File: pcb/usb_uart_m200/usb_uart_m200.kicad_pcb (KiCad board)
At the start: 2 copper layers, 25 x 25.1 mm, 17 parts, among them J1 Conn_01x02_Socket, P1 USB_C_Plug_USB2.0, U1 CY7C65213-28PVXI, U2 MIC5317-3.3xM5, U4 USBLC6-2SC6, X1 2059-301_998-403

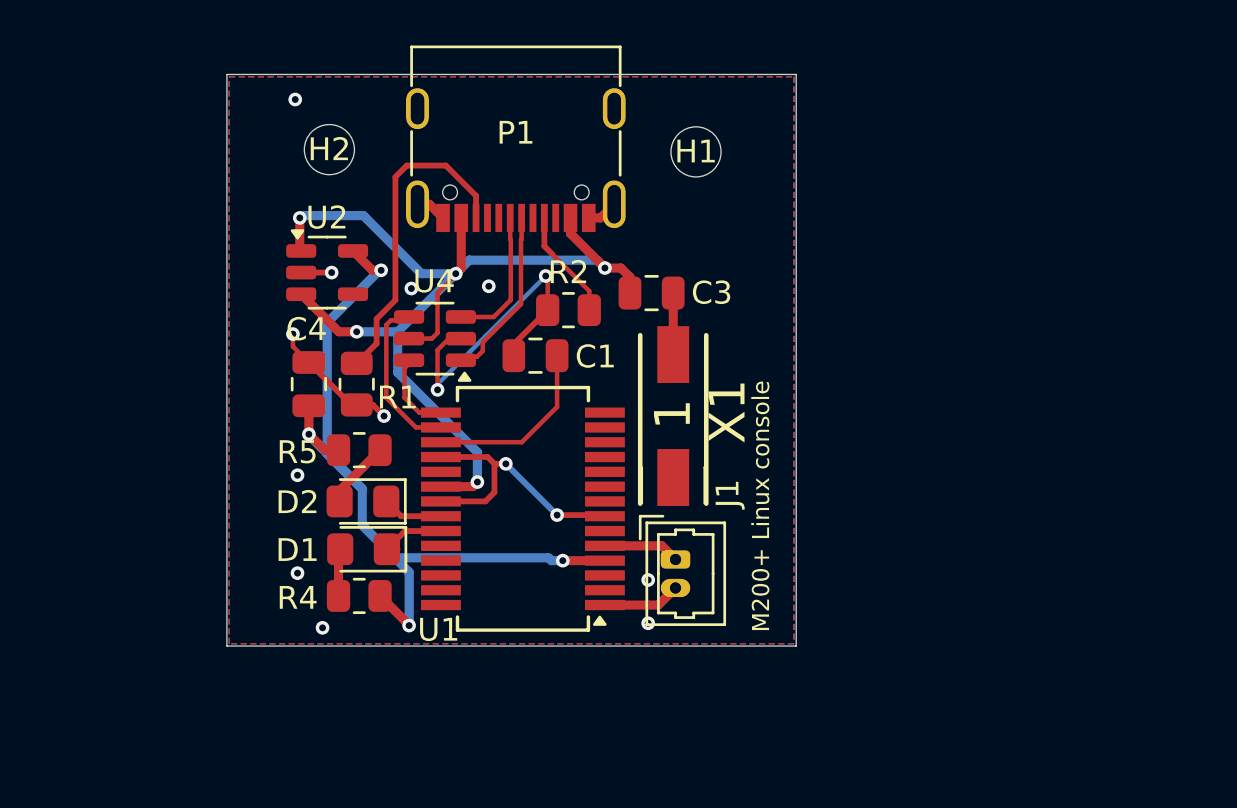
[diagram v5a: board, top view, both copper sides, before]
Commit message: Updating the uart and fel mode adapter after soldering it.
Manufacturing shiwed the pcb to be too large and the gnd wire connector
too close to the uart connector. The farnell reference resistor on the
fel mode adapter was of the wrong foorprint.
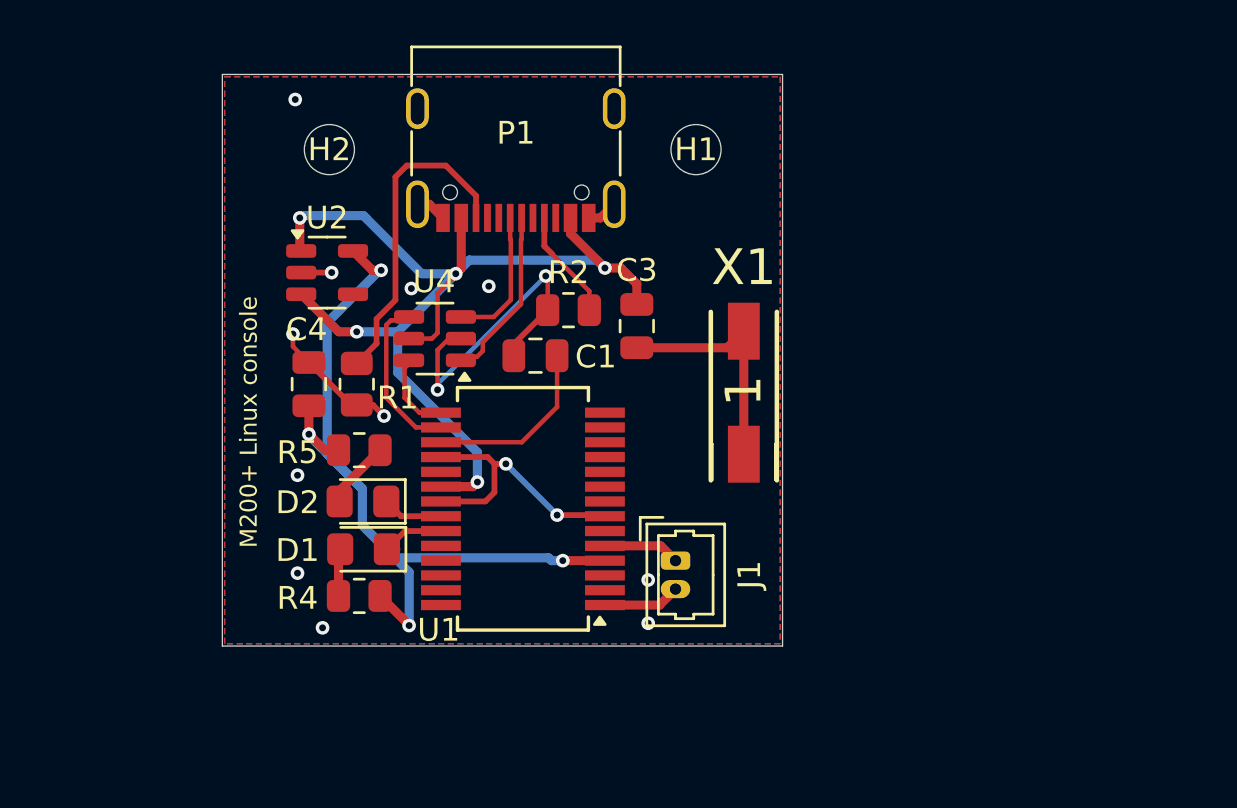
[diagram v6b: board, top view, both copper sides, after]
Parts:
- moved X1 3.27 mm to (169.7, 67.8)
- moved C3 1.59 mm to (165.0, 65.0), turned to -90 degrees
- moved H1 0.10 mm to (167.6, 57.2)
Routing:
- net GND: track 38.7 -> 47.2 mm
- net /VBUS: track 46.3 -> 46.9 mm
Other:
- board size 25 x 25.1 mm -> 24.6 x 25.1 mm
